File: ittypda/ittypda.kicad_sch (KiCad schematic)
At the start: 146 parts, among them J1 USB_C_Receptacle_USB2.0_14P, SW1 SW_SPDT, U1 STM32F401RETx, U2 BQ24040DSQR, U3 TLV75801PDRV, Y1 16Mhz

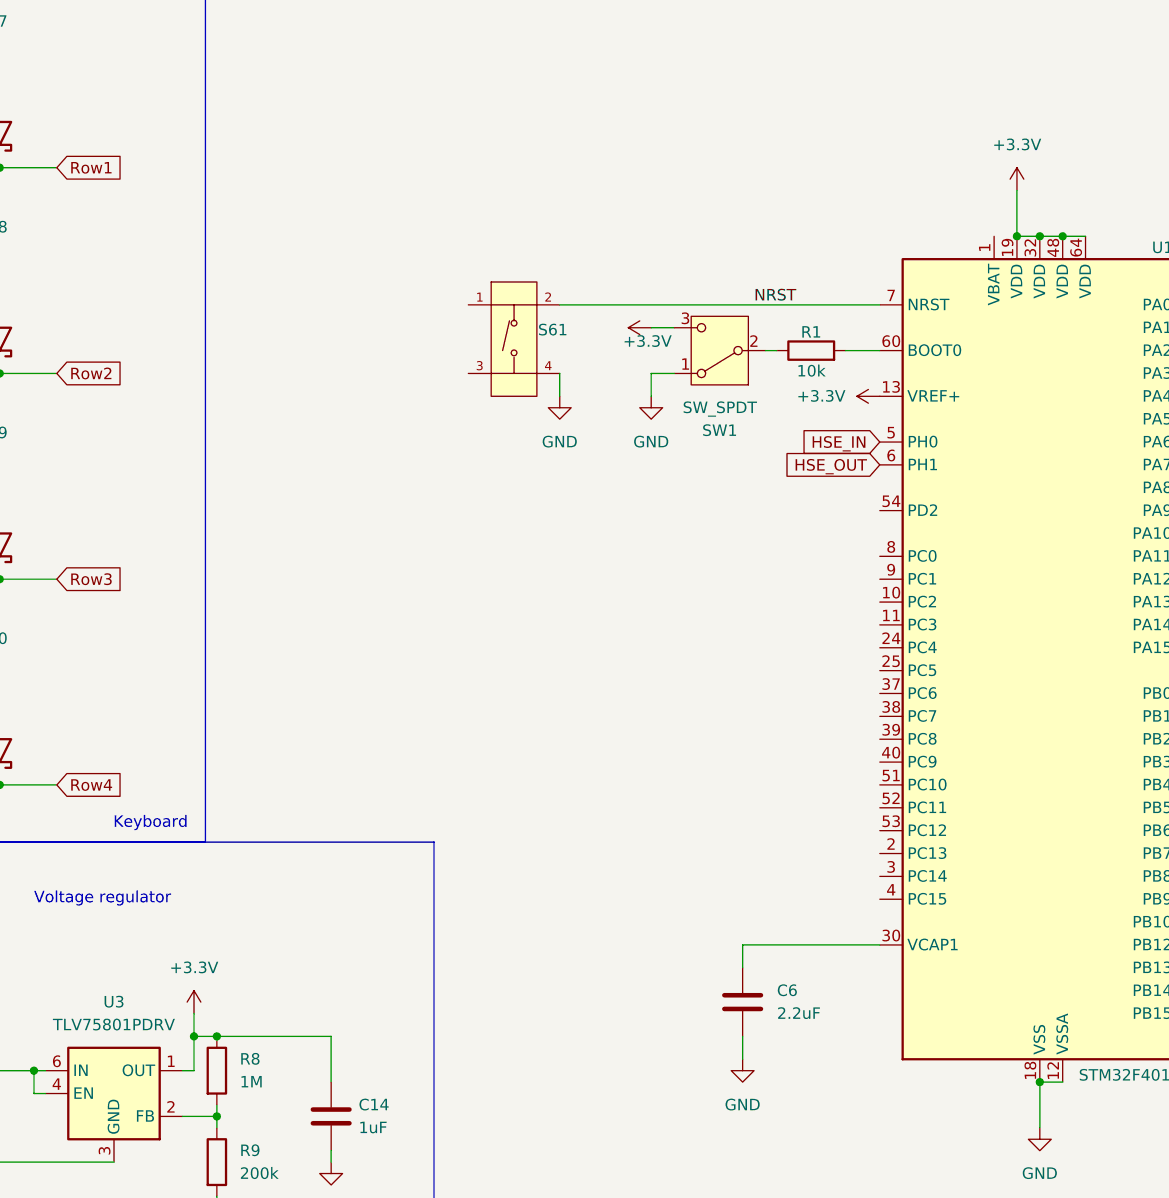
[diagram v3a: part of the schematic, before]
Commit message: wire up VBAT
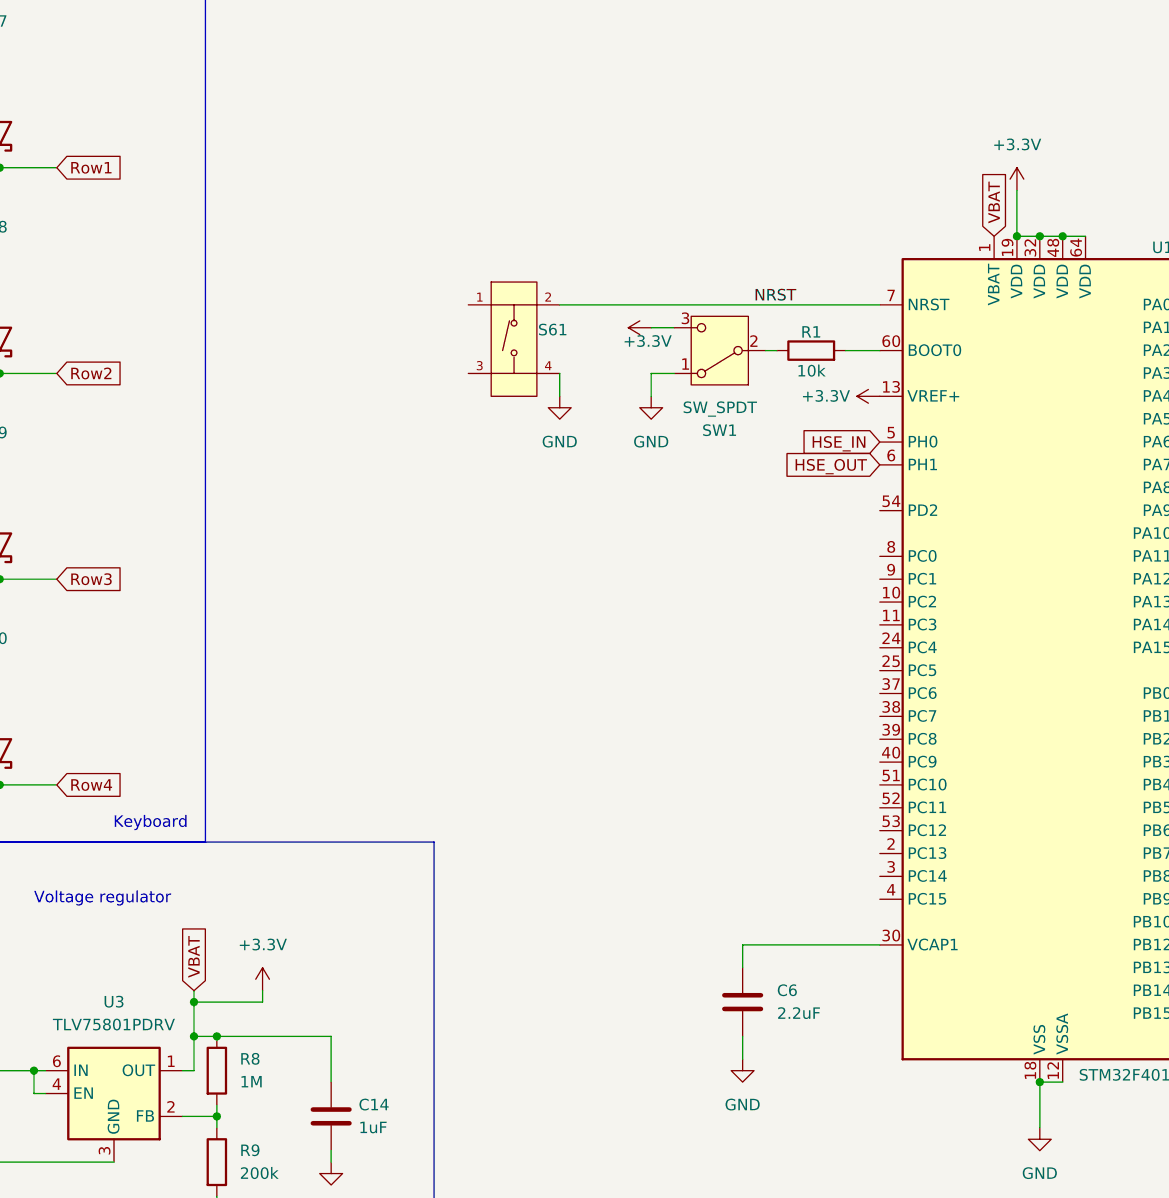
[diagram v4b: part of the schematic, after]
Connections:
- net +3.3V: now also U1.1 (VBAT)
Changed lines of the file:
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@@
 	)
 	(junction
+		(at 209.55 170.18)
+		(diameter 0)
+		(color 0 0 0 0)
+	)
+	(junction
 		(at 187.96 146.05)
 		(diameter 0)
@@
 	)
 	(junction
+		(at 209.55 173.99)
+		(diameter 0)
+		(color 0 0 0 0)
+	)
+	(junction
 		(at 104.14 77.47)
 		(diameter 0)
@@
 	)
 	(junction
-		(at 209.55 173.99)
-		(diameter 0)
-		(color 0 0 0 0)
-	)
-	(junction
 		(at 300.99 85.09)
 		(diameter 0)
@@
 	(wire
 		(pts
-			(xy 209.55 171.45) (xy 209.55 173.99)
+			(xy 209.55 168.91) (xy 209.55 170.18)
 		)
 		(stroke
@@
 	(wire
 		(pts
+			(xy 217.17 168.91) (xy 217.17 170.18)
+		)
+		(stroke
+			(width 0)
+			(type default)
+		)
+	)
+	(wire
+		(pts
 			(xy 22.86 35.56) (xy 22.86 58.42)
 		)
@@
 	(wire
 		(pts
+			(xy 217.17 170.18) (xy 209.55 170.18)
+		)
+		(stroke
+			(width 0)
+			(type default)
+		)
+	)
+	(wire
+		(pts
 			(xy 50.8 58.42) (xy 50.8 81.28)
 		)
@@
 	(wire
 		(pts
+			(xy 209.55 170.18) (xy 209.55 173.99)
+		)
+		(stroke
+			(width 0)
+			(type default)
+		)
+	)
+	(wire
+		(pts
 			(xy 83.82 175.26) (xy 83.82 173.99)
 		)
@@
 		)
 	)
+	(global_label "VBAT"
+		(shape input)
+		(at 298.45 85.09 90)
+		(fields_autoplaced yes)
+		(effects
+			(font
+				(size 1.27 1.27)
+			)
+			(justify left)
+		)
+		(property "Intersheetrefs" "${INTERSHEET_REFS}"
+			(at 298.45 77.69 90)
+			(hide yes)
+			(show_name no)
+			(do_not_autoplace no)
+			(effects
+				(font
+					(size 1.27 1.27)
+				)
+				(justify left)
+			)
+		)
+	)
 	(global_label "BAT+"
 		(shape input)
@@
 		)
 	)
+	(global_label "VBAT"
+		(shape input)
+		(at 209.55 168.91 90)
+		(fields_autoplaced yes)
+		(effects
+			(font
+				(size 1.27 1.27)
+			)
+			(justify left)
+		)
+		(property "Intersheetrefs" "${INTERSHEET_REFS}"
+			(at 209.55 161.51 90)
+			(hide yes)
+			(show_name no)
+			(do_not_autoplace no)
+			(effects
+				(font
+					(size 1.27 1.27)
+				)
+				(justify left)
+			)
+		)
+	)
 	(global_label "Row1"
 		(shape input)
@@
 		(in_pos_files yes)
 		(dnp no)
-		(fields_autoplaced yes)
 		(property "Reference" "#PWR013"
 			(at 289.56 102.87 0)
@@
 		)
 		(property "Value" "+3.3V"
-			(at 281.94 102.8699 90)
+			(at 282.448 102.87 90)
 			(show_name no)
 			(do_not_autoplace no)
@@
 	)
 	(symbol
-		(lib_id "power:+3.3V")
-		(at 209.55 171.45 0)
-		(unit 1)
-		(body_style 1)
-		(exclude_from_sim no)
-		(in_bom yes)
-		(on_board yes)
-		(in_pos_files yes)
-		(dnp no)
-		(fields_autoplaced yes)
-		(property "Reference" "#PWR021"
-			(at 209.55 175.26 0)
-			(hide yes)
-			(show_name no)
-			(do_not_autoplace no)
-			(effects
-				(font
-					(size 1.27 1.27)
-				)
-			)
-		)
-		(property "Value" "+3.3V"
-			(at 209.55 166.37 0)
-			(show_name no)
-			(do_not_autoplace no)
-			(effects
-				(font
-					(size 1.27 1.27)
-				)
-			)
-		)
-		(property "Footprint" ""
-			(at 209.55 171.45 0)
-			(hide yes)
-			(show_name no)
-			(do_not_autoplace no)
-			(effects
-				(font
-					(size 1.27 1.27)
-				)
-			)
-		)
-		(property "Datasheet" ""
-			(at 209.55 171.45 0)
-			(hide yes)
-			(show_name no)
-			(do_not_autoplace no)
-			(effects
-				(font
-					(size 1.27 1.27)
-				)
-			)
-		)
-		(property "Description" "Power symbol creates a global label with name \"+3.3V\""
-			(at 209.55 171.45 0)
-			(hide yes)
-			(show_name no)
-			(do_not_autoplace no)
-			(effects
-				(font
-					(size 1.27 1.27)
-				)
-			)
-		)
-		(pin "1"
-		)
-		(instances
-			(project "ittypda"
-				(path "/d1aa8f6c-1644-4347-b86d-2b771500f753"
-					(reference "#PWR021")
-					(unit 1)
-				)
-			)
-		)
-	)
-	(symbol
 		(lib_id "Device:C")
 		(at 242.57 40.64 0)
@@
 					(unit 1)
 				)
+			)
+		)
+	)
+	(symbol
+		(lib_id "power:+3.3V")
+		(at 217.17 168.91 0)
+		(unit 1)
+		(body_style 1)
+		(exclude_from_sim no)
+		(in_bom yes)
+		(on_board yes)
+		(in_pos_files yes)
+		(dnp no)
+		(fields_autoplaced yes)
+		(property "Reference" "#PWR021"
+			(at 217.17 172.72 0)
+			(hide yes)
+			(show_name no)
+			(do_not_autoplace no)
+			(effects
+				(font
+					(size 1.27 1.27)
+				)
+			)
+		)
+		(property "Value" "+3.3V"
+			(at 217.17 163.83 0)
+			(show_name no)
+			(do_not_autoplace no)
+			(effects
+				(font
+					(size 1.27 1.27)
+				)
+			)
+		)
+		(property "Footprint" ""
+			(at 217.17 168.91 0)
+			(hide yes)
+			(show_name no)
+			(do_not_autoplace no)
+			(effects
+				(font
+					(size 1.27 1.27)
+				)
+			)
+		)
+		(property "Datasheet" ""
+			(at 217.17 168.91 0)
+			(hide yes)
+			(show_name no)
+			(do_not_autoplace no)
+			(effects
+				(font
+					(size 1.27 1.27)
+				)
+			)
+		)
+		(property "Description" "Power symbol creates a global label with name \"+3.3V\""
+			(at 217.17 168.91 0)
+			(hide yes)
+			(show_name no)
+			(do_not_autoplace no)
+			(effects
+				(font
+					(size 1.27 1.27)
+				)
+			)
+		)
+		(pin "1"
+		)
+		(instances
+			(project "ittypda"
+				(path "/d1aa8f6c-1644-4347-b86d-2b771500f753"
+					(reference "#PWR021")
+					(unit 1)
+				)

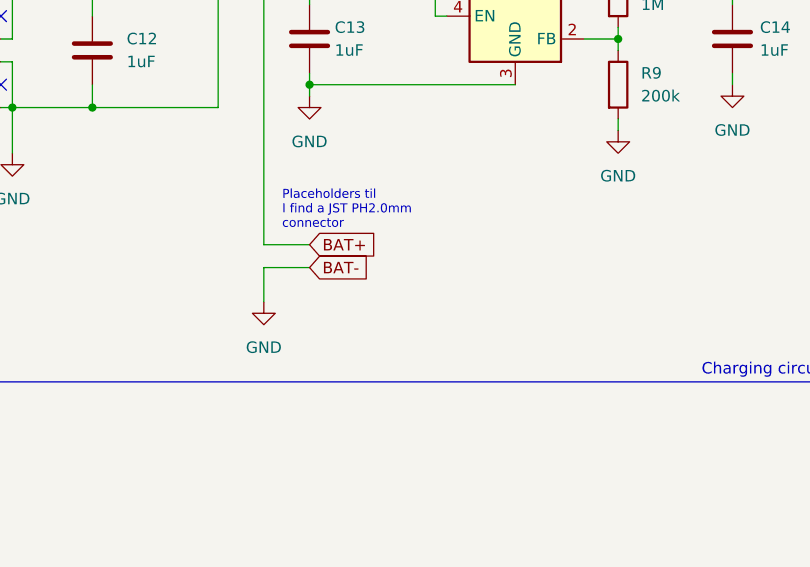
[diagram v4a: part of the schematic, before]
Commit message: add JST connector
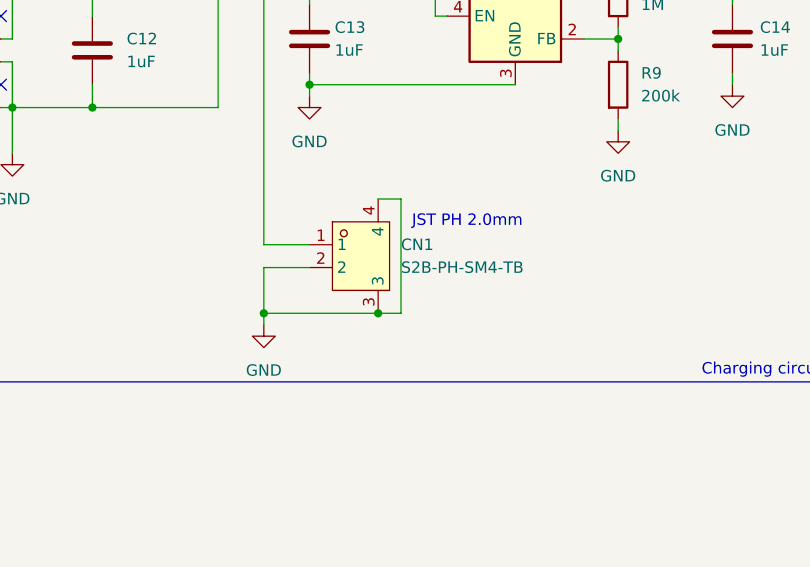
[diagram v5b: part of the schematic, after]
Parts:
- added CN1: S2B-PH-SM4-TB, easyeda2kicad:CONN-SMD_P2.00_S2B-PH-SM4-TB-LF-SN, symbol easyeda2kicad:S2B-PH-SM4-TB
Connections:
- net GND: now also CN1.2, CN1.3, CN1.4
- net BAT+: no longer names the net of C12.1, C13.1, U2.10 (OUT), U3.4 (EN), U3.6 (IN)
- net BAT+: now also CN1.1
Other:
- note added: "JST PH 2.0mm"
- note removed: "Placeholders til I find a JST PH2.0mm connector"
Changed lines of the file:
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@@
 		)
 	)
-	(text "Placeholders til\nI find a JST PH2.0mm\nconnector"
-		(exclude_from_sim no)
-		(at 174.752 201.93 0)
-		(effects
-			(font
-				(size 1 1)
-			)
-			(justify left)
-		)
-	)
 	(text "Disconnected since the display\ndoesn't have the touch module.\nThese 4 pins are I2C for\nthe touch module\n"
 		(exclude_from_sim no)
@@
 		)
 	)
+	(text "JST PH 2.0mm"
+		(exclude_from_sim no)
+		(at 195.326 203.2 0)
+		(effects
+			(font
+				(size 1.27 1.27)
+			)
+		)
+	)
 	(text "USB-C"
 		(exclude_from_sim no)
@@
 	)
 	(junction
+		(at 185.42 213.36)
+		(diameter 0)
+		(color 0 0 0 0)
+	)
+	(junction
 		(at 90.17 54.61)
 		(diameter 0)
@@
 	)
 	(junction
+		(at 172.72 213.36)
+		(diameter 0)
+		(color 0 0 0 0)
+	)
+	(junction
 		(at 90.17 77.47)
 		(diameter 0)
@@
 	(wire
 		(pts
+			(xy 172.72 214.63) (xy 172.72 213.36)
+		)
+		(stroke
+			(width 0)
+			(type default)
+		)
+	)
+	(wire
+		(pts
 			(xy 36.83 104.14) (xy 36.83 127)
 		)
@@
 	(wire
 		(pts
+			(xy 172.72 213.36) (xy 185.42 213.36)
+		)
+		(stroke
+			(width 0)
+			(type default)
+		)
+	)
+	(wire
+		(pts
 			(xy 177.8 35.56) (xy 176.53 35.56)
 		)
@@
 	(wire
 		(pts
+			(xy 187.96 200.66) (xy 187.96 213.36)
+		)
+		(stroke
+			(width 0)
+			(type default)
+		)
+	)
+	(wire
+		(pts
 			(xy 100.33 182.88) (xy 100.33 196.85)
 		)
@@
 	(wire
 		(pts
-			(xy 172.72 212.09) (xy 172.72 208.28)
+			(xy 172.72 213.36) (xy 172.72 208.28)
 		)
 		(stroke
@@
 	(wire
 		(pts
+			(xy 185.42 200.66) (xy 187.96 200.66)
+		)
+		(stroke
+			(width 0)
+			(type default)
+		)
+	)
+	(wire
+		(pts
 			(xy 300.99 80.01) (xy 300.99 85.09)
 		)
@@
 	(wire
 		(pts
+			(xy 187.96 213.36) (xy 185.42 213.36)
+		)
+		(stroke
+			(width 0)
+			(type default)
+		)
+	)
+	(wire
+		(pts
 			(xy 76.2 43.18) (xy 76.2 46.99)
 		)
@@
 		)
 	)
-	(global_label "BAT+"
-		(shape input)
-		(at 177.8 205.74 0)
-		(fields_autoplaced yes)
-		(effects
-			(font
-				(size 1.27 1.27)
-			)
-			(justify left)
-		)
-		(property "Intersheetrefs" "${INTERSHEET_REFS}"
-			(at 185.6838 205.74 0)
-			(hide yes)
-			(show_name no)
-			(do_not_autoplace no)
-			(effects
-				(font
-					(size 1.27 1.27)
-				)
-				(justify left)
-			)
-		)
-	)
 	(global_label "Col3"
 		(shape input)
@@
 		)
 	)
-	(global_label "BAT-"
-		(shape input)
-		(at 177.8 208.28 0)
-		(fields_autoplaced yes)
-		(effects
-			(font
-				(size 1.27 1.27)
-			)
-			(justify left)
-		)
-		(property "Intersheetrefs" "${INTERSHEET_REFS}"
-			(at 185.6838 208.28 0)
-			(hide yes)
-			(show_name no)
-			(do_not_autoplace no)
-			(effects
-				(font
-					(size 1.27 1.27)
-				)
-				(justify left)
-			)
-		)
-	)
 	(global_label "Col6"
 		(shape input)
@@
 	)
 	(symbol
+		(lib_id "easyeda2kicad:S2B-PH-SM4-TB")
+		(at 181.61 207.01 0)
+		(unit 1)
+		(body_style 1)
+		(exclude_from_sim no)
+		(in_bom yes)
+		(on_board yes)
+		(in_pos_files yes)
+		(dnp no)
+		(fields_autoplaced yes)
+		(property "Reference" "CN1"
+			(at 187.96 205.7399 0)
+			(show_name no)
+			(do_not_autoplace no)
+			(effects
+				(font
+					(size 1.27 1.27)
+				)
+				(justify left)
+			)
+		)
+		(property "Value" "S2B-PH-SM4-TB"
+			(at 187.96 208.2799 0)
+			(show_name no)
+			(do_not_autoplace no)
+			(effects
+				(font
+					(size 1.27 1.27)
+				)
+				(justify left)
+			)
+		)
+		(property "Footprint" "easyeda2kicad:CONN-SMD_P2.00_S2B-PH-SM4-TB-LF-SN"
+			(at 181.61 220.98 0)
+			(hide yes)
+			(show_name no)
+			(do_not_autoplace no)
+			(effects
+				(font
+					(size 1.27 1.27)
+				)
+			)
+		)
+		(property "Datasheet" "https://lcsc.com/product-detail/_JST-Sales-America_S2B-PH-SM4-TB-LF-SN_JST-Sales-America-S2B-PH-SM4-TB-LF-SN_C295747.html"
+			(at 181.61 223.52 0)
+			(hide yes)
+			(show_name no)
+			(do_not_autoplace no)
+			(effects
+				(font
+					(size 1.27 1.27)
+				)
+			)
+		)
+		(property "Description" ""
+			(at 181.61 207.01 0)
+			(hide yes)
+			(show_name no)
+			(do_not_autoplace no)
+			(effects
+				(font
+					(size 1.27 1.27)
+				)
+			)
+		)
+		(property "Manufacturer" "JST"
+			(at 181.61 226.06 0)
+			(hide yes)
+			(show_name no)
+			(do_not_autoplace no)
+			(effects
+				(font
+					(size 1.27 1.27)
+				)
+			)
+		)
+		(property "MPN" "S2B-PH-SM4-TB(LF)(SN)"
+			(at 181.61 228.6 0)
+			(hide yes)
+			(show_name no)
+			(do_not_autoplace no)
+			(effects
+				(font
+					(size 1.27 1.27)
+				)
+			)
+		)
+		(property "LCSC Part" "C295747"
+			(at 181.61 231.14 0)
+			(hide yes)
+			(show_name no)
+			(do_not_autoplace no)
+			(effects
+				(font
+					(size 1.27 1.27)
+				)
+			)
+		)
+		(pin "1"
+		)
+		(pin "3"
+		)
+		(pin "2"
+		)
+		(pin "4"
+		)
+		(instances
+			(project "ittypda"
+				(path "/d1aa8f6c-1644-4347-b86d-2b771500f753"
+					(reference "CN1")
+					(unit 1)
+				)
+			)
+		)
+	)
+	(symbol
 		(lib_id "PCM_JLCPCB-Diodes:Schottky,1N5819WS")
 		(at 104.14 96.52 0)
@@
 	(symbol
 		(lib_id "power:GND")
-		(at 172.72 212.09 0)
+		(at 172.72 214.63 0)
 		(unit 1)
 		(body_style 1)
@@
 		(fields_autoplaced yes)
 		(property "Reference" "#PWR022"
-			(at 172.72 218.44 0)
+			(at 172.72 220.98 0)
 			(hide yes)
 			(show_name no)
@@
 		)
 		(property "Value" "GND"
-			(at 172.72 217.17 0)
+			(at 172.72 219.71 0)
 			(show_name no)
 			(do_not_autoplace no)
@@
 		)
 		(property "Footprint" ""
-			(at 172.72 212.09 0)
+			(at 172.72 214.63 0)
 			(hide yes)
 			(show_name no)
@@
 		)
 		(property "Datasheet" ""
-			(at 172.72 212.09 0)
+			(at 172.72 214.63 0)
 			(hide yes)
 			(show_name no)
@@
 		)
 		(property "Description" "Power symbol creates a global label with name \"GND\" , ground"
-			(at 172.72 212.09 0)
+			(at 172.72 214.63 0)
 			(hide yes)
 			(show_name no)
